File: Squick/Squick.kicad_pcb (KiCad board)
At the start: 2 copper layers, 91.5 x 92 mm, 104 parts, among them J1 BT, J10 D24V3F-5V, J2 DEBUG UART, J3 PROG, J4 VL53L0X_L, J5 VL53L0X_F, J6 VL53L0X_R, J7 ENK_L, J8 ENK_R, J9 BATT, Q1 AO3407A, Q2 AO3407A, SW1 USER_BUT_1, SW2 USER_BUT_2, SW3 RESET, SW4 ON/OFF, T1 SFH-313FA, T2 SFH-313FA, T3 SFH-313FA, T4 SFH-313FA, T5 SFH-313FA, T6 SFH-313FA, U1 STM32F411RETx, U10 LM1117-3.3, U2 CD4051B, U3 KTIR0711S, U4 CD4051B, U5 KTIR0711S, U6 KTIR0711S, U7 KTIR0711S, U8 Adafruit_4554, U9 TB6612FNG

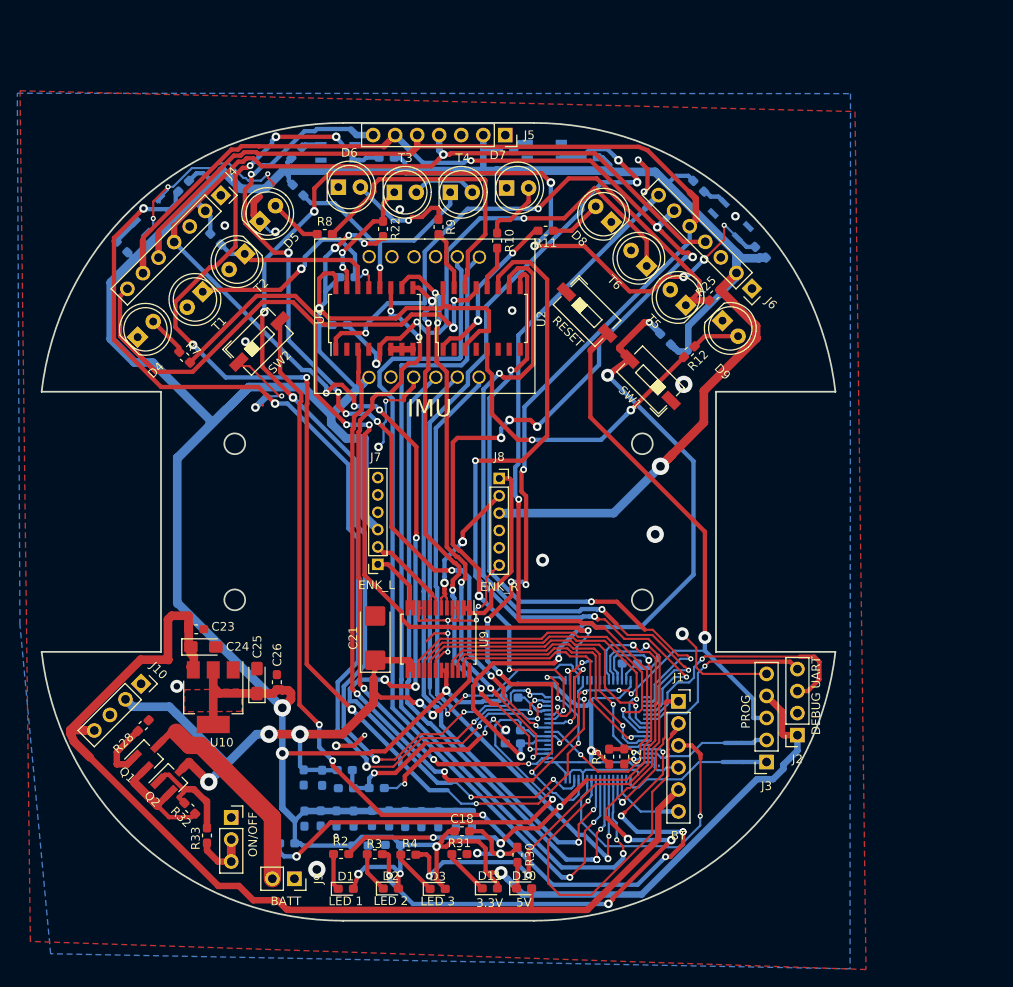
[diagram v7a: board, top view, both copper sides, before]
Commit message: 3 GND connections to go
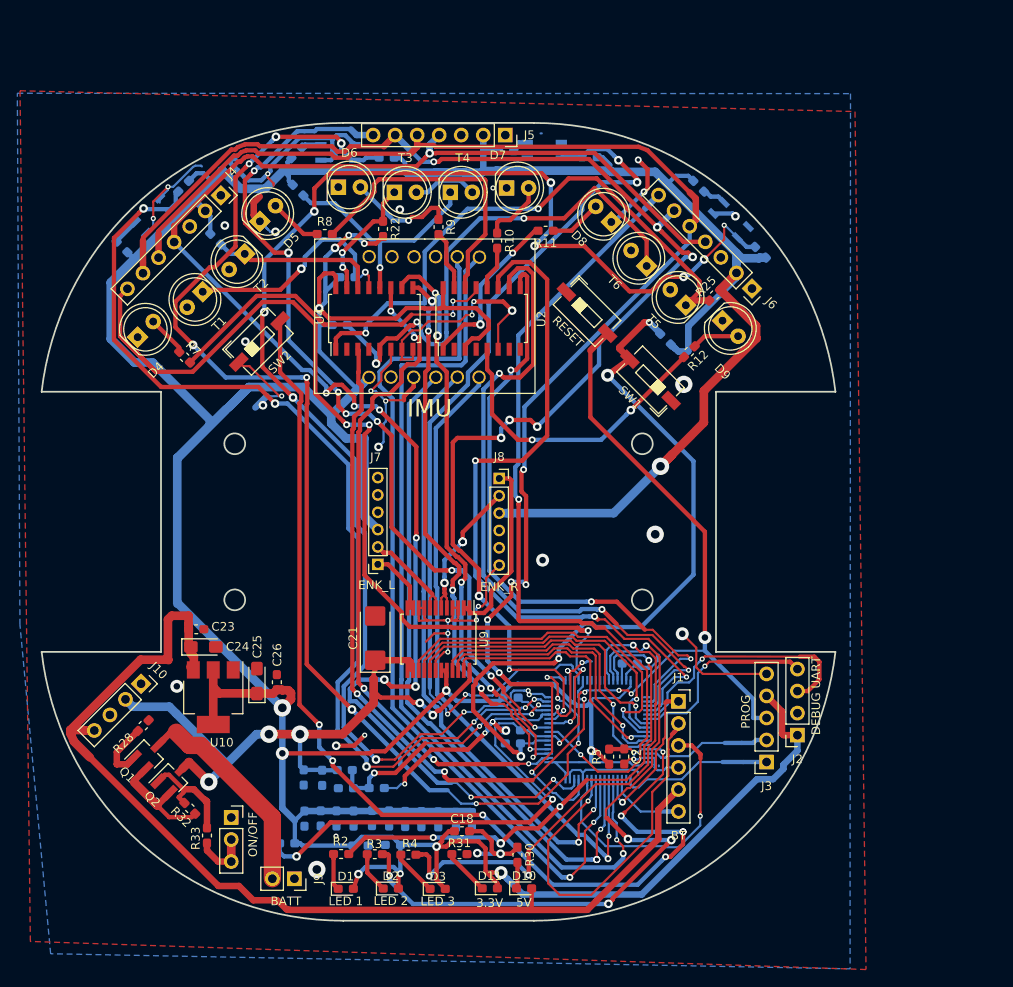
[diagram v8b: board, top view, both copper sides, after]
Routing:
- net GND: track 183.6 -> 250.6 mm, vias 40 -> 44
- net IR_1: track 45.2 -> 40.5 mm
- net PT_6: track 59.1 -> 60.7 mm
- net V_batt: track 30.7 -> 29.5 mm
- net RESET: track 134.4 -> 133.4 mm
- net +3.3V: track 620.8 -> 620.0 mm
- net KTIR_1: track 117.8 -> 117.1 mm
- net VL_XSHUT: track 161.9 -> 162.6 mm
- net SCL: track 168.9 -> 169.6 mm
- net (no net): track 0.16 -> 0.31 mm, vias 0 -> 1
- removed copper zone on F.Cu, net +3.3V
